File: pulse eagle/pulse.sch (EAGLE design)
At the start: 24 parts, among them IC1 LM358D, J1 ISP Touch, T1 BC846, Y1 8MHz

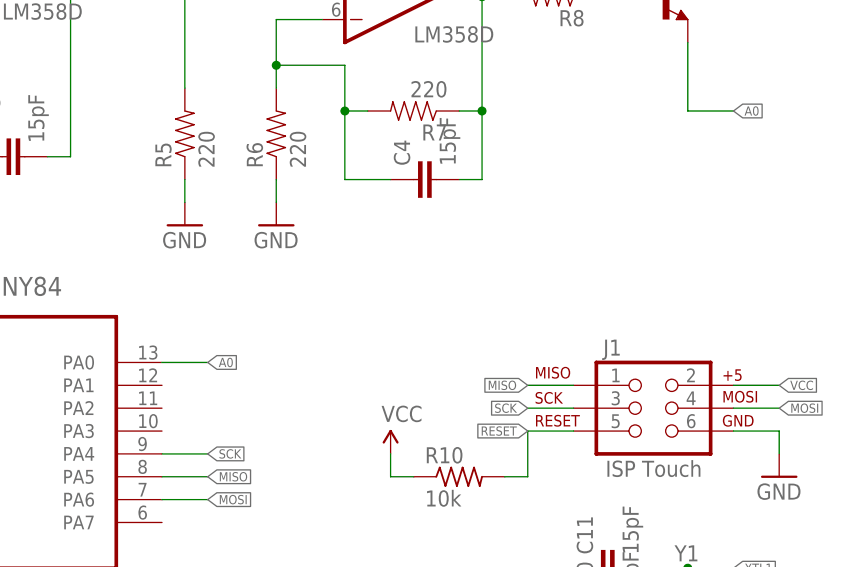
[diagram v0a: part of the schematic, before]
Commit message: Adding serial port headers.
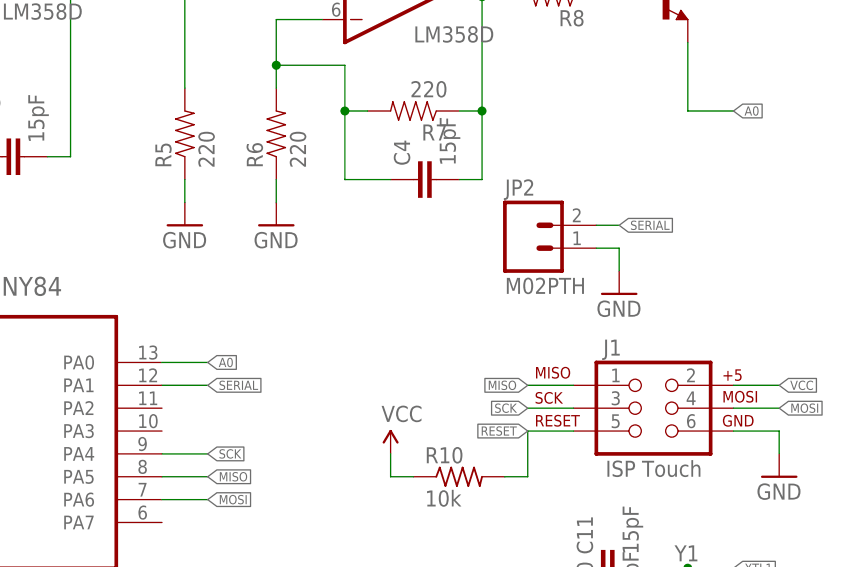
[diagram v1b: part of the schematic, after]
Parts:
- added JP2: M02PTH, SparkFun-Connectors:M02PTH
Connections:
- new net SERIAL: ATTINY84.PA1, JP2.2
- net GND: now also JP2.1
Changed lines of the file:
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@@
 <part name="SUPPLY6" library="SparkFun-Aesthetics" deviceset="VCC" device=""/>
 <part name="GND10" library="SparkFun" deviceset="GND" device=""/>
+<part name="JP2" library="SparkFun-Connectors" deviceset="M02" device="PTH"/>
+<part name="GND11" library="SparkFun" deviceset="GND" device=""/>
 </parts>
 <sheets>
@@
 <instance part="SUPPLY6" gate="1" x="104.14" y="22.86"/>
 <instance part="GND10" gate="1" x="147.32" y="20.32"/>
+<instance part="JP2" gate="G$1" x="119.38" y="45.72"/>
+<instance part="GND11" gate="1" x="129.54" y="40.64"/>
 </instances>
 <busses>
@@
 <wire x1="142.24" y1="25.4" x2="147.32" y2="25.4" width="0.1524" layer="91"/>
 <wire x1="147.32" y1="25.4" x2="147.32" y2="22.86" width="0.1524" layer="91"/>
+</segment>
+<segment>
+<pinref part="JP2" gate="G$1" pin="1"/>
+<wire x1="127" y1="45.72" x2="129.54" y2="45.72" width="0.1524" layer="91"/>
+<wire x1="129.54" y1="45.72" x2="129.54" y2="43.18" width="0.1524" layer="91"/>
+<pinref part="GND11" gate="1" pin="GND"/>
 </segment>
 </net>
@@
 </segment>
 </net>
+<net name="SERIAL" class="0">
+<segment>
+<pinref part="ATTINY84" gate="A" pin="PA1"/>
+<wire x1="78.74" y1="30.48" x2="83.82" y2="30.48" width="0.1524" layer="91"/>
+<label x="83.82" y="30.48" size="1.016" layer="95" xref="yes"/>
+</segment>
+<segment>
+<wire x1="127" y1="48.26" x2="129.54" y2="48.26" width="0.1524" layer="91"/>
+<label x="129.54" y="48.26" size="1.016" layer="95" xref="yes"/>
+<pinref part="JP2" gate="G$1" pin="2"/>
+</segment>
+</net>

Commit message: Rev. A of the board.
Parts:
- C1, C3: value .1uf -> 1uf
- C12: value .1uf -> .1uF
- C2, C4: value 15pF -> .1uF
- R2: value 220 -> 39k
- R3, R5: value 220 -> 68k
- R4: value 220 -> 8.2k
- R6: value 220 -> 1k
- R7: value 220 -> 470k
- R8: value 220 -> 1.8k
- T1: value BC846 -> MMBT3904
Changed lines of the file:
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@@
 <parts>
 <part name="ATTINY84" library="Atmel_By_element14_Batch_1" deviceset="ATTINY84-20SSU" device="" value=""/>
-<part name="C12" library="adafruit" deviceset="C-US" device="C0805" value=".1uf"/>
+<part name="C12" library="adafruit" deviceset="C-US" device="C0805" value=".1uF"/>
 <part name="R10" library="adafruit" deviceset="R-US_" device="R0805" value="10k"/>
 <part name="Y1" library="remote" deviceset="CRYSTAL" device="" value="8MHz"/>
@@
 <part name="CN1" library="adafruit" deviceset="JST_2PIN" device="-THM"/>
 <part name="R1" library="SparkFun-Resistors" deviceset="220-5%" device="" value="220"/>
-<part name="R2" library="SparkFun-Resistors" deviceset="220-5%" device="" value="220"/>
-<part name="R3" library="SparkFun-Resistors" deviceset="220-5%" device="" value="220"/>
-<part name="R4" library="SparkFun-Resistors" deviceset="220-5%" device="" value="220"/>
-<part name="R5" library="SparkFun-Resistors" deviceset="220-5%" device="" value="220"/>
-<part name="R6" library="SparkFun-Resistors" deviceset="220-5%" device="" value="220"/>
-<part name="R7" library="SparkFun-Resistors" deviceset="220-5%" device="" value="220"/>
-<part name="R8" library="SparkFun-Resistors" deviceset="220-5%" device="" value="220"/>
-<part name="C1" library="adafruit" deviceset="C-US" device="C0805" value=".1uf"/>
-<part name="C3" library="adafruit" deviceset="C-US" device="C0805" value=".1uf"/>
-<part name="C2" library="SparkFun-Passives" deviceset="CAP" device="0805" value="15pF"/>
-<part name="C4" library="SparkFun-Passives" deviceset="CAP" device="0805" value="15pF"/>
-<part name="T1" library="transistor" deviceset="BC846" device=""/>
+<part name="R2" library="SparkFun-Resistors" deviceset="220-5%" device="" value="39k"/>
+<part name="R3" library="SparkFun-Resistors" deviceset="220-5%" device="" value="68k"/>
+<part name="R4" library="SparkFun-Resistors" deviceset="220-5%" device="" value="8.2k"/>
+<part name="R5" library="SparkFun-Resistors" deviceset="220-5%" device="" value="68k"/>
+<part name="R6" library="SparkFun-Resistors" deviceset="220-5%" device="" value="1k"/>
+<part name="R7" library="SparkFun-Resistors" deviceset="220-5%" device="" value="470k"/>
+<part name="R8" library="SparkFun-Resistors" deviceset="220-5%" device="" value="1.8k"/>
+<part name="C1" library="adafruit" deviceset="C-US" device="C0805" value="1uf"/>
+<part name="C3" library="adafruit" deviceset="C-US" device="C0805" value="1uf"/>
+<part name="C2" library="SparkFun-Passives" deviceset="CAP" device="0805" value=".1uF"/>
+<part name="C4" library="SparkFun-Passives" deviceset="CAP" device="0805" value=".1uF"/>
+<part name="T1" library="transistor" deviceset="BC846" device="" value="MMBT3904"/>
 <part name="IC1" library="linear" deviceset="LM358" device="D"/>
 <part name="GND1" library="SparkFun" deviceset="GND" device=""/>
@@
 <instance part="SUPPLY4" gate="1" x="58.42" y="86.36"/>
 <instance part="SUPPLY5" gate="1" x="27.94" y="35.56"/>
-<instance part="GND9" gate="1" x="35.56" y="10.16"/>
+<instance part="GND9" gate="1" x="27.94" y="10.16"/>
 <instance part="SUPPLY6" gate="1" x="104.14" y="22.86"/>
 <instance part="GND10" gate="1" x="147.32" y="20.32"/>
@@
 <segment>
 <pinref part="ATTINY84" gate="A" pin="GND"/>
-<wire x1="43.18" y1="15.24" x2="35.56" y2="15.24" width="0.1524" layer="91"/>
-<wire x1="35.56" y1="15.24" x2="35.56" y2="12.7" width="0.1524" layer="91"/>
+<wire x1="43.18" y1="15.24" x2="27.94" y2="15.24" width="0.1524" layer="91"/>
+<wire x1="27.94" y1="15.24" x2="27.94" y2="12.7" width="0.1524" layer="91"/>
 <pinref part="C12" gate="G$1" pin="2"/>
 <wire x1="27.94" y1="20.32" x2="27.94" y2="15.24" width="0.1524" layer="91"/>
-<junction x="35.56" y="15.24"/>
-<wire x1="27.94" y1="15.24" x2="35.56" y2="15.24" width="0.1524" layer="91"/>
+<junction x="27.94" y="15.24"/>
 <junction x="27.94" y="15.24"/>
 <wire x1="27.94" y1="15.24" x2="15.24" y2="15.24" width="0.1524" layer="91"/>

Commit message: Moving pins around.
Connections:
- net A0: now also ATTINY84.PA1; no longer ATTINY84.PA0
- net SERIAL: now also ATTINY84.PA2; no longer ATTINY84.PA1
- net VCC: now also ATTINY84.PA0
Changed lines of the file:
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@@
 <layer number="112" name="tSilk" color="7" fill="1" visible="yes" active="yes"/>
 <layer number="116" name="Patch_BOT" color="9" fill="4" visible="yes" active="yes"/>
+<layer number="118" name="Rect_Pads" color="7" fill="1" visible="no" active="no"/>
 <layer number="121" name="_tsilk" color="7" fill="1" visible="yes" active="yes"/>
 <layer number="122" name="_bsilk" color="7" fill="1" visible="yes" active="yes"/>
@@
 <part name="JP2" library="SparkFun-Connectors" deviceset="M02" device="PTH"/>
 <part name="GND11" library="SparkFun" deviceset="GND" device=""/>
+<part name="SUPPLY7" library="SparkFun-Aesthetics" deviceset="VCC" device=""/>
 </parts>
 <sheets>
@@
 <instance part="JP2" gate="G$1" x="119.38" y="45.72"/>
 <instance part="GND11" gate="1" x="129.54" y="40.64"/>
+<instance part="SUPPLY7" gate="1" x="83.82" y="35.56"/>
 </instances>
 <busses>
@@
 <pinref part="SUPPLY4" gate="1" pin="VCC"/>
 <wire x1="58.42" y1="83.82" x2="58.42" y2="86.36" width="0.1524" layer="91"/>
+</segment>
+<segment>
+<pinref part="ATTINY84" gate="A" pin="PA0"/>
+<wire x1="78.74" y1="33.02" x2="83.82" y2="33.02" width="0.1524" layer="91"/>
+<wire x1="83.82" y1="33.02" x2="83.82" y2="35.56" width="0.1524" layer="91"/>
+<pinref part="SUPPLY7" gate="1" pin="VCC"/>
 </segment>
 </net>
@@
 <net name="A0" class="0">
 <segment>
-<pinref part="ATTINY84" gate="A" pin="PA0"/>
-<wire x1="78.74" y1="33.02" x2="83.82" y2="33.02" width="0.1524" layer="91"/>
-<label x="83.82" y="33.02" size="1.016" layer="95" xref="yes"/>
-</segment>
-<segment>
 <pinref part="T1" gate="G$1" pin="E"/>
 <wire x1="137.16" y1="68.58" x2="137.16" y2="60.96" width="0.1524" layer="91"/>
@@
 <label x="142.24" y="60.96" size="1.016" layer="95" xref="yes"/>
 </segment>
-</net>
-<net name="SERIAL" class="0">
 <segment>
 <pinref part="ATTINY84" gate="A" pin="PA1"/>
@@
 <label x="83.82" y="30.48" size="1.016" layer="95" xref="yes"/>
 </segment>
+</net>
+<net name="SERIAL" class="0">
 <segment>
 <wire x1="127" y1="48.26" x2="129.54" y2="48.26" width="0.1524" layer="91"/>
@@
 <pinref part="JP2" gate="G$1" pin="2"/>
 </segment>
-</net>
+<segment>
+<pinref part="ATTINY84" gate="A" pin="PA2"/>
+<wire x1="78.74" y1="27.94" x2="83.82" y2="27.94" width="0.1524" layer="91"/>
+<label x="83.82" y="27.94" size="1.016" layer="95" xref="yes"/>
+</segment>
+</net>

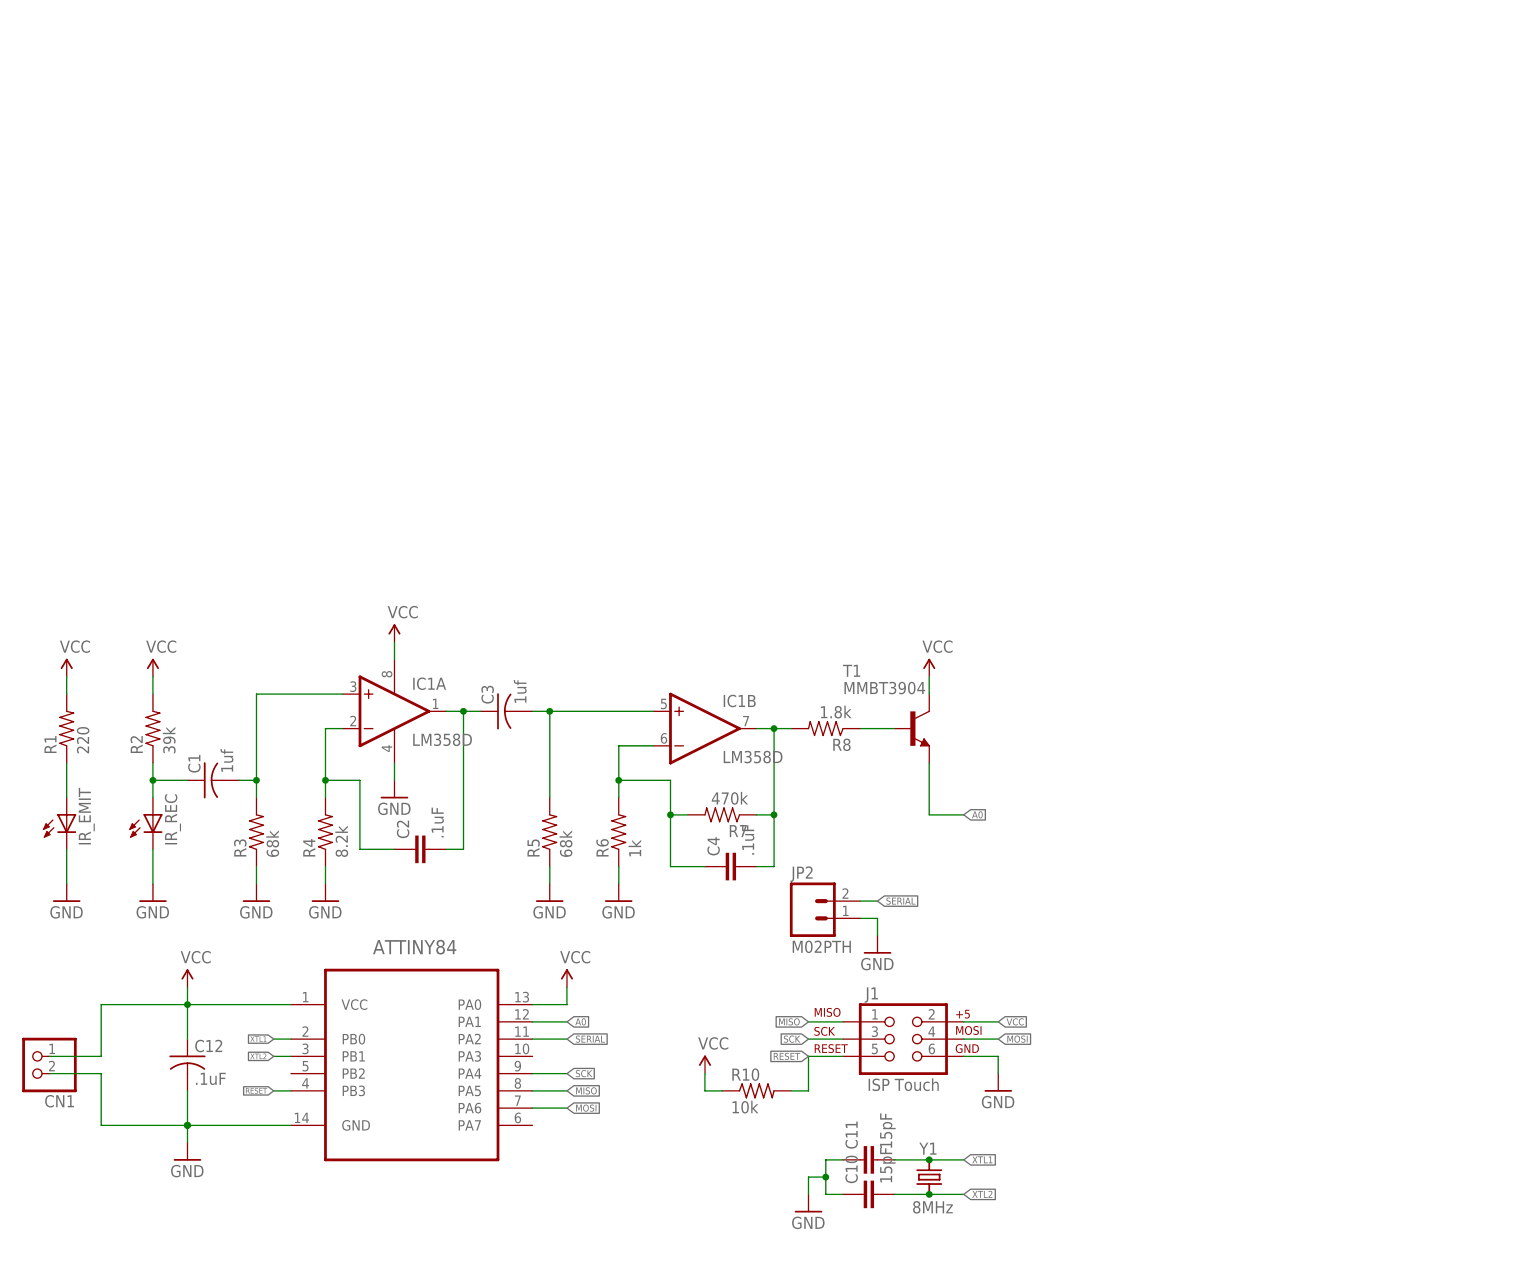
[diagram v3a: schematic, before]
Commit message: Rev. 2 of the board, with new headers for el wire, led data, and pwm led.
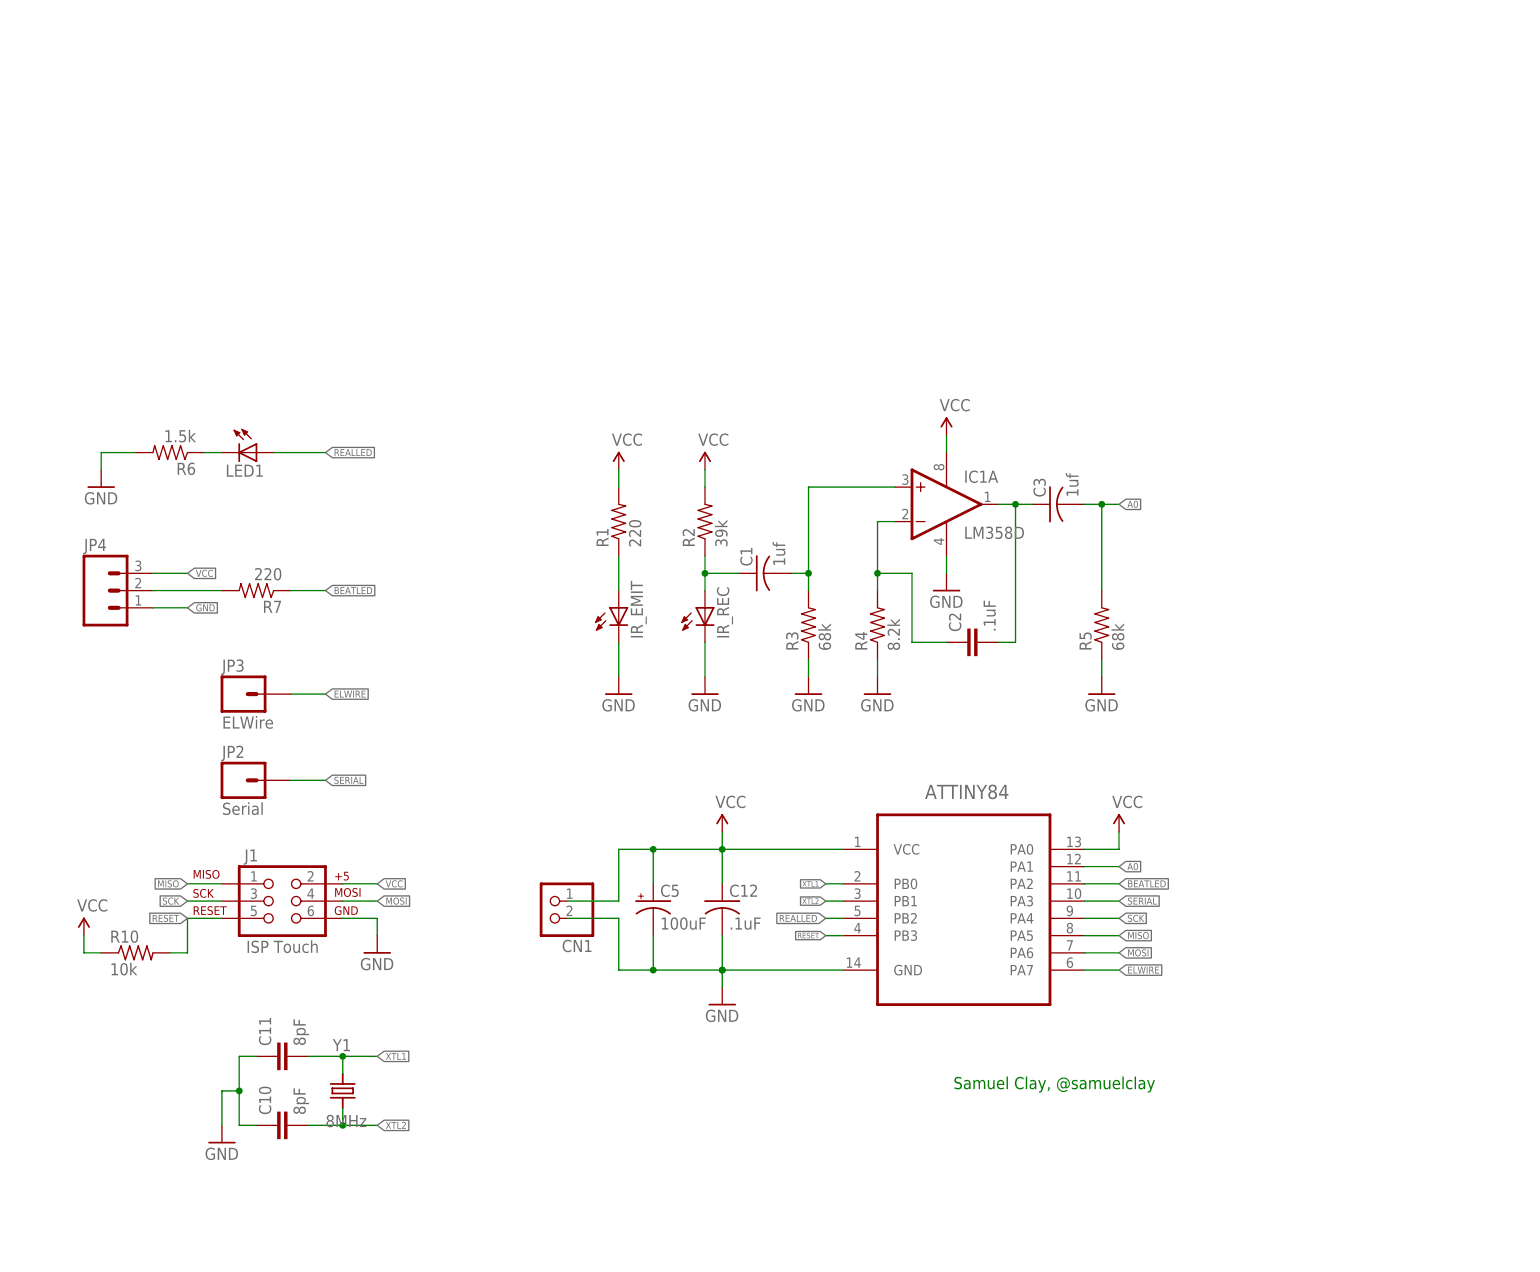
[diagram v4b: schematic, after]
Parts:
- removed C4: .1uF, SparkFun-Passives:CAP0805
- removed R8: 1.8k, SparkFun-Resistors:220-5%
- removed T1: MMBT3904, transistor:BC846
- added C5: 100uF, SparkFun-Capacitors:10UF-16V-10%(TANT)
- added JP3: ELWire, SparkFun-Connectors:M01PTH
- added JP4: (no value), SparkFun-Connectors:M03PTH
- added LED1: (no value), SparkFun-LED:LED0603
- C10, C11: value 15pF -> 8pF
- JP2: value M02PTH -> Serial; device SparkFun-Connectors:M02PTH -> SparkFun-Connectors:M01PTH
- R6: value 1k -> 1.5k
- R7: value 470k -> 220
- Y1: device remote:CRYSTAL -> remote:CRYSTAL5X3.2
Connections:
- removed net N$6: C3.2, IC1B.+IN, R5.2
- removed net N$9: R8.1, T1.B
- new net BEATLED: ATTINY84.PA2, R7.1
- new net ELWIRE: ATTINY84.PA7, JP3.1
- new net REALLED: ATTINY84.PB2, LED1.A
- net A0: now also C3.2, R5.2; no longer T1.E
- net GND: now also C5.-, JP4.1, R6.2; no longer JP2.1, R6.1
- net N$7: now also JP4.2; no longer C4.1, IC1B.-IN, R6.2
- net N$8: now also LED1.C, R6.1; no longer C4.2, IC1B.OUT, R7.1, R8.2
- net SERIAL: now also ATTINY84.PA3, JP2.1; no longer ATTINY84.PA2, JP2.2
- net VCC: now also C5.+, JP4.3; no longer T1.C
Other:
- note added: "Samuel Clay, @samuelclay"
- moved on the sheet: ATTINY84, C1, C10, C11, C12, C2, C3, CN1, IC1A, IR_EMIT, IR_REC, J1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
